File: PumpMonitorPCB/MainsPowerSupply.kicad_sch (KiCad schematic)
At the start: 31 parts, among them K1 J115F11CH5VDCS61-5U, Q1 AS2302, U1 ACS770xCB-050B-PFF, U2 AMS1117-3.3, U3 LMV321, U4 LMV321

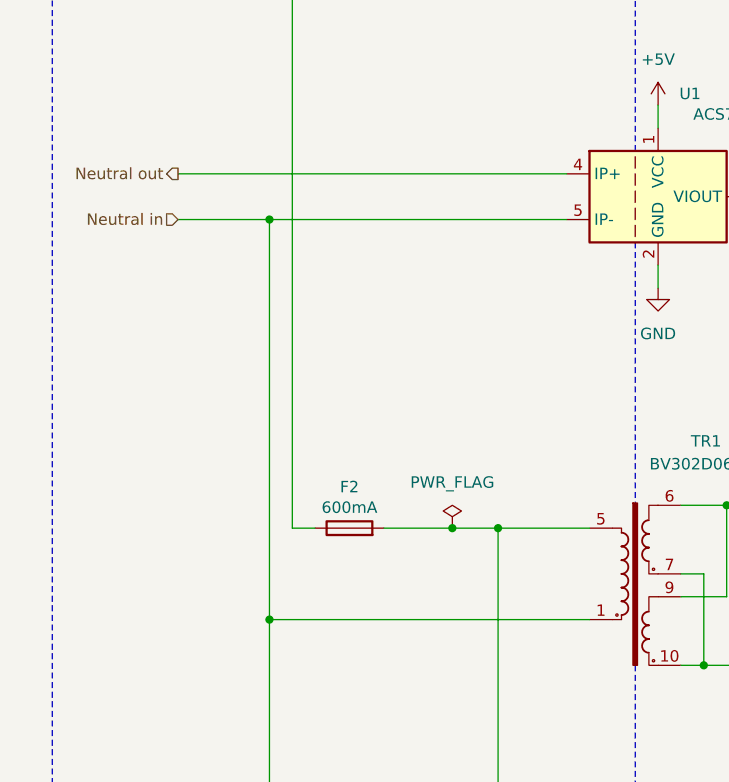
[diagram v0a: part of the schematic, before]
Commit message: Added fuse on aux relay, setting creepage and clearance distances.
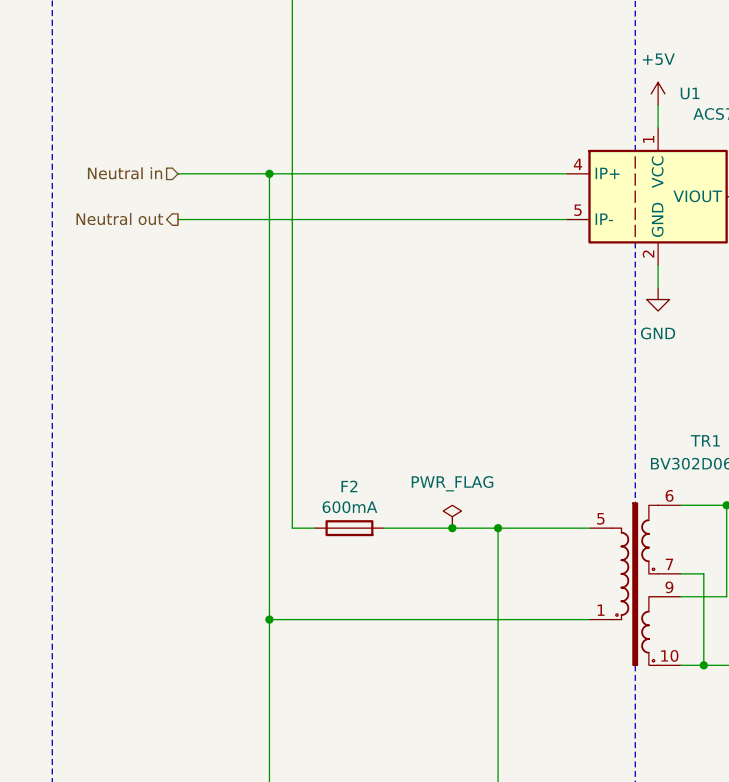
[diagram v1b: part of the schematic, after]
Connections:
- net Neutral in: now also U1.4 (IP+); no longer U1.5 (IP-)
- net Neutral out: now also U1.5 (IP-); no longer U1.4 (IP+)
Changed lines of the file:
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@@
-	)
-	(junction
-		(at 38.1 92.71)
-		(diameter 0)
-		(color 0 0 0 0)
 	)
 	(junction
@@
 	)
 	(junction
+		(at 38.1 87.63)
+		(diameter 0)
+		(color 0 0 0 0)
+	)
+	(junction
 		(at 124.46 142.24)
 		(diameter 0)
@@
 	(wire
 		(pts
-			(xy 27.94 87.63) (xy 71.12 87.63)
-		)
-		(stroke
-			(width 0)
-			(type default)
-		)
-	)
-	(wire
-		(pts
 			(xy 92.71 180.34) (xy 92.71 182.88)
 		)
@@
 	(wire
 		(pts
-			(xy 27.94 92.71) (xy 38.1 92.71)
+			(xy 27.94 87.63) (xy 38.1 87.63)
 		)
 		(stroke
@@
 	(wire
 		(pts
-			(xy 38.1 92.71) (xy 71.12 92.71)
+			(xy 38.1 87.63) (xy 71.12 87.63)
 		)
 		(stroke
@@
 	(wire
 		(pts
+			(xy 38.1 87.63) (xy 38.1 137.16)
+		)
+		(stroke
+			(width 0)
+			(type default)
+		)
+	)
+	(wire
+		(pts
 			(xy 95.25 142.24) (xy 113.03 142.24)
 		)
@@
 	(wire
 		(pts
+			(xy 27.94 92.71) (xy 71.12 92.71)
+		)
+		(stroke
+			(width 0)
+			(type default)
+		)
+	)
+	(wire
+		(pts
 			(xy 146.05 177.8) (xy 146.05 180.34)
 		)
@@
 		(pts
 			(xy 144.78 92.71) (xy 147.32 92.71)
-		)
-		(stroke
-			(width 0)
-			(type default)
-		)
-	)
-	(wire
-		(pts
-			(xy 38.1 92.71) (xy 38.1 137.16)
 		)
 		(stroke
@@
 	(hierarchical_label "Neutral out"
 		(shape output)
-		(at 27.94 87.63 180)
+		(at 27.94 92.71 180)
 		(effects
 			(font
@@
 	(hierarchical_label "Neutral in"
 		(shape input)
-		(at 27.94 92.71 180)
+		(at 27.94 87.63 180)
 		(effects
 			(font
@@
 		(length 2.54)
 		(shape round)
+		(at 30.48 87.63 0)
+		(fields_autoplaced yes)
+		(effects
+			(font
+				(size 1.27 1.27)
+			)
+			(justify left bottom)
+		)
+		(property "Netclass" "HV_{N}"
+			(at 31.1785 85.09 0)
+			(effects
+				(font
+					(size 1.27 1.27)
+				)
+				(justify left)
+			)
+		)
+		(property "Component Class" ""
+			(at -93.98 49.53 0)
+			(effects
+				(font
+					(size 1.27 1.27)
+					(italic yes)
+				)
+			)
+		)
+	)
+	(netclass_flag ""
+		(length 2.54)
+		(shape round)
 		(at 30.48 92.71 0)
 		(fields_autoplaced yes)
@@
 			(effects
 				(font
-					(size 1.27 1.27)
-					(italic yes)
-				)
-			)
-		)
-	)
-	(netclass_flag ""
-		(length 2.54)
-		(shape round)
-		(at 30.48 87.63 0)
-		(fields_autoplaced yes)
-		(effects
-			(font
-				(size 1.27 1.27)
-			)
-			(justify left bottom)
-		)
-		(property "Netclass" "HV_{N}"
-			(at 31.1785 85.09 0)
-			(effects
-				(font
-					(size 1.27 1.27)
-				)
-				(justify left)
-			)
-		)
-		(property "Component Class" ""
-			(at -93.98 49.53 0)
-			(effects
-				(font

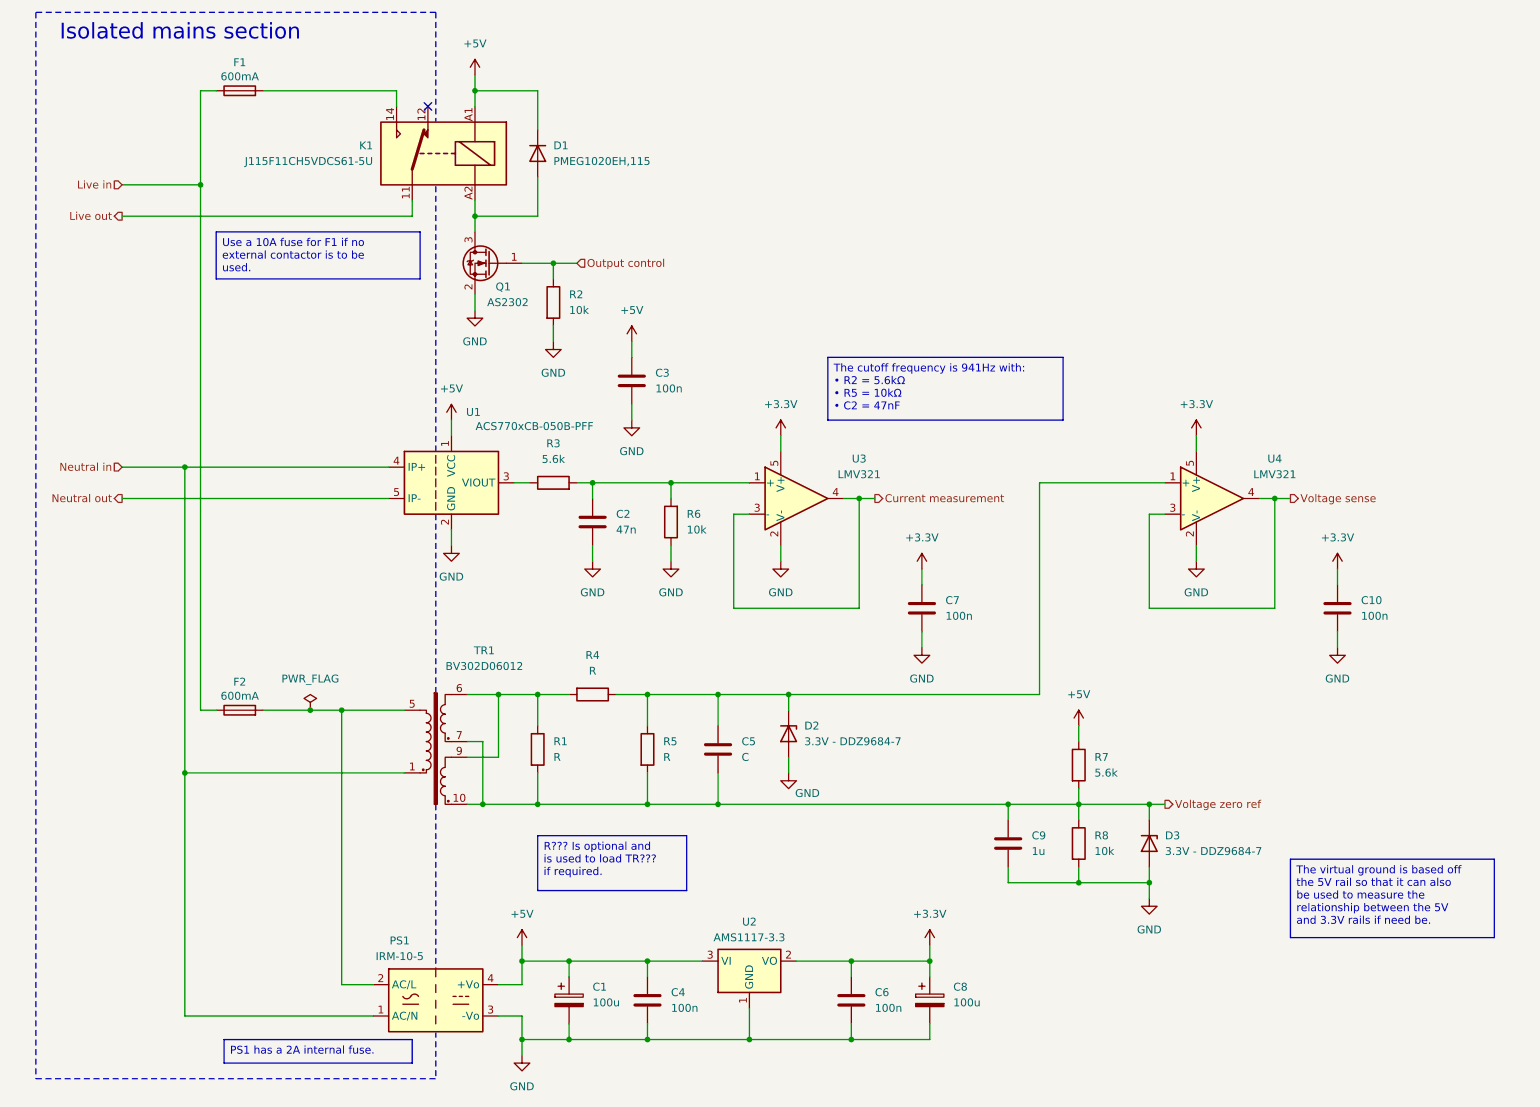
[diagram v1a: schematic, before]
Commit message: Adding test points, CAD files
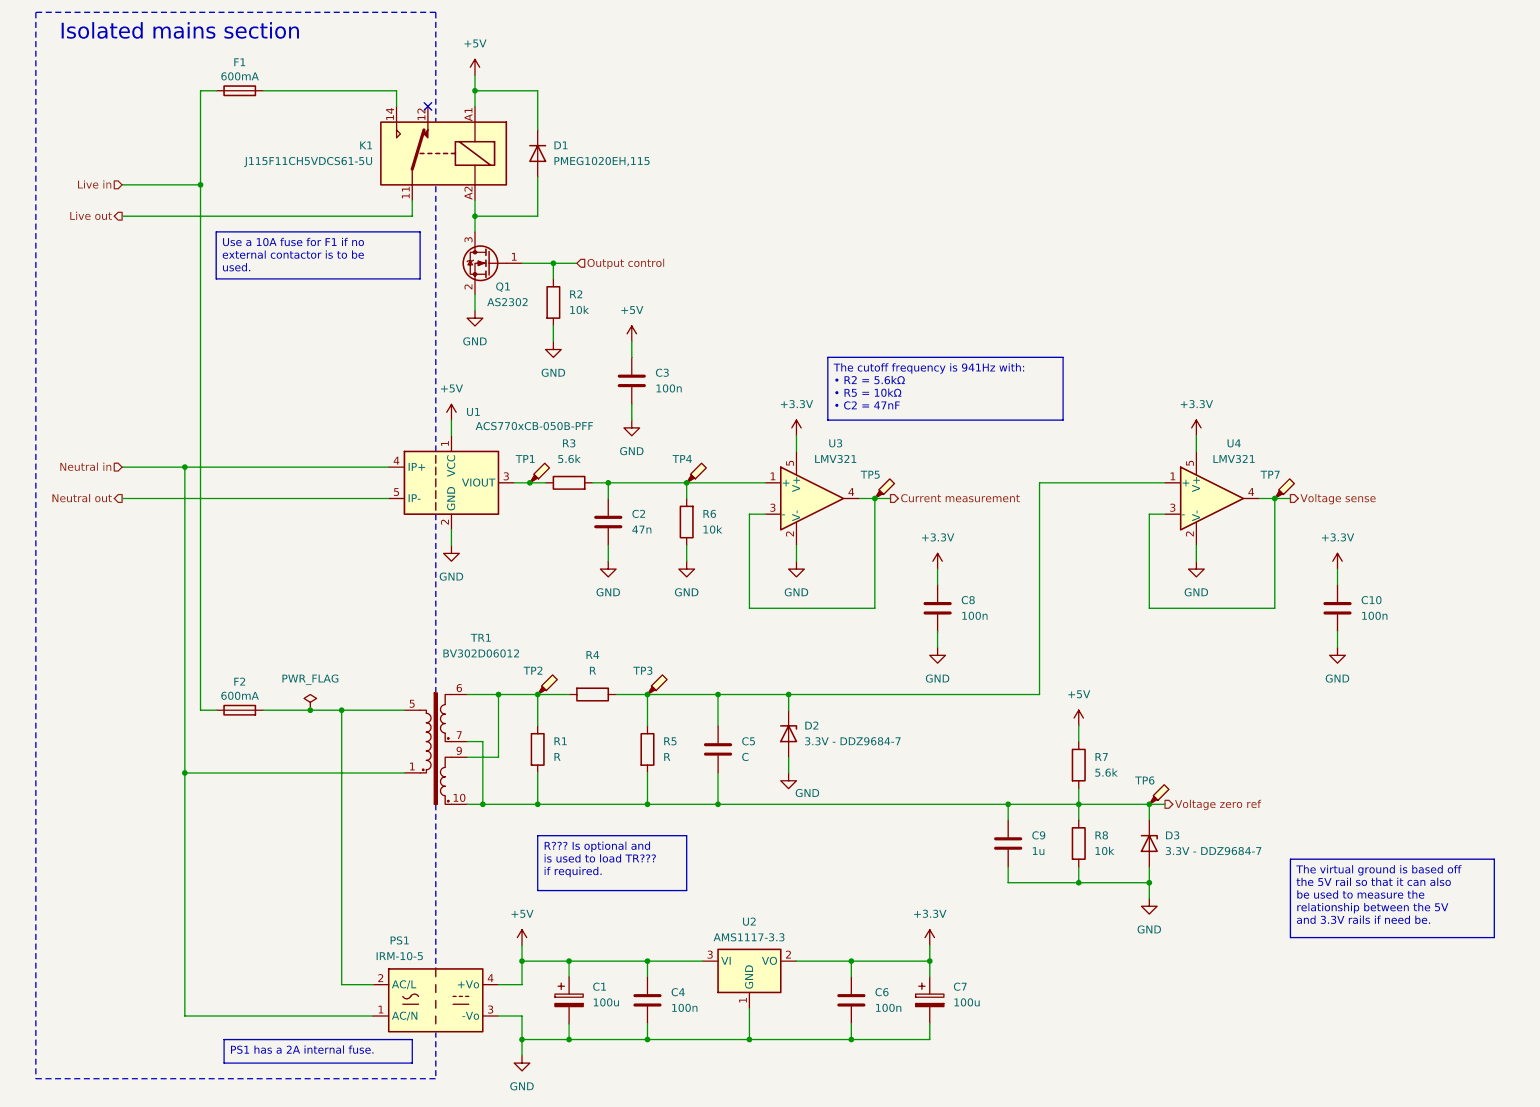
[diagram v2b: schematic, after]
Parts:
- added TP1, TP2, TP3, TP4, TP5, TP6, TP7: ~, TestPoint:TestPoint_THTPad_D1.5mm_Drill0.7mm, symbol Connector:TestPoint_Probe
- C10, C3, C4, C6: DigikeyNumber (none) -> 311-1088-1-ND
- C2: DigikeyNumber (none) -> 1276-2079-1-ND
- C8: renamed from C7; DigikeyNumber (none) -> 311-1088-1-ND
- C9: DigikeyNumber (none) -> 587-1241-1-ND
- D1: DigikeyNumber (none) -> 1727-3849-1-ND
- D2, D3: DigikeyNumber (none) -> DDZ9684-7DICT-ND
- F1, F2: DigikeyNumber (none) -> 732-11372-ND
- K1: DigikeyNumber (none) -> 2449-J115F11CH5VDCS61.5U-ND
- PS1: DigikeyNumber (none) -> 1866-3032-ND
- Q1: DigikeyNumber (none) -> 4530-AS2302CT-ND
- renumbered C8 to C7
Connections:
- net Current measurement: now also TP5.1
- net Voltage sense: now also TP7.1
- net Voltage zero ref: now also TP6.1
- net at C5.1, D2.1 (K), R4.1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: now also TP3.1
- net at C2.1, R3.2, R6.2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: now also TP4.1
- net at R1.1, R4.2, TR1.6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: now also TP2.1
- net at R3.1, U1.3 (VIOUT): now also TP1.1
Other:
- moved on the sheet: C2, C8, R3, R6, U3
